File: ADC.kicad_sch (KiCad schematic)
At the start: 5 parts, among them J1 Conn_01x03_Socket, J11 Conn_01x03_Socket, J12 Conn_01x03_Socket, J13 Conn_01x03_Socket, U4 ADS1115IDGS

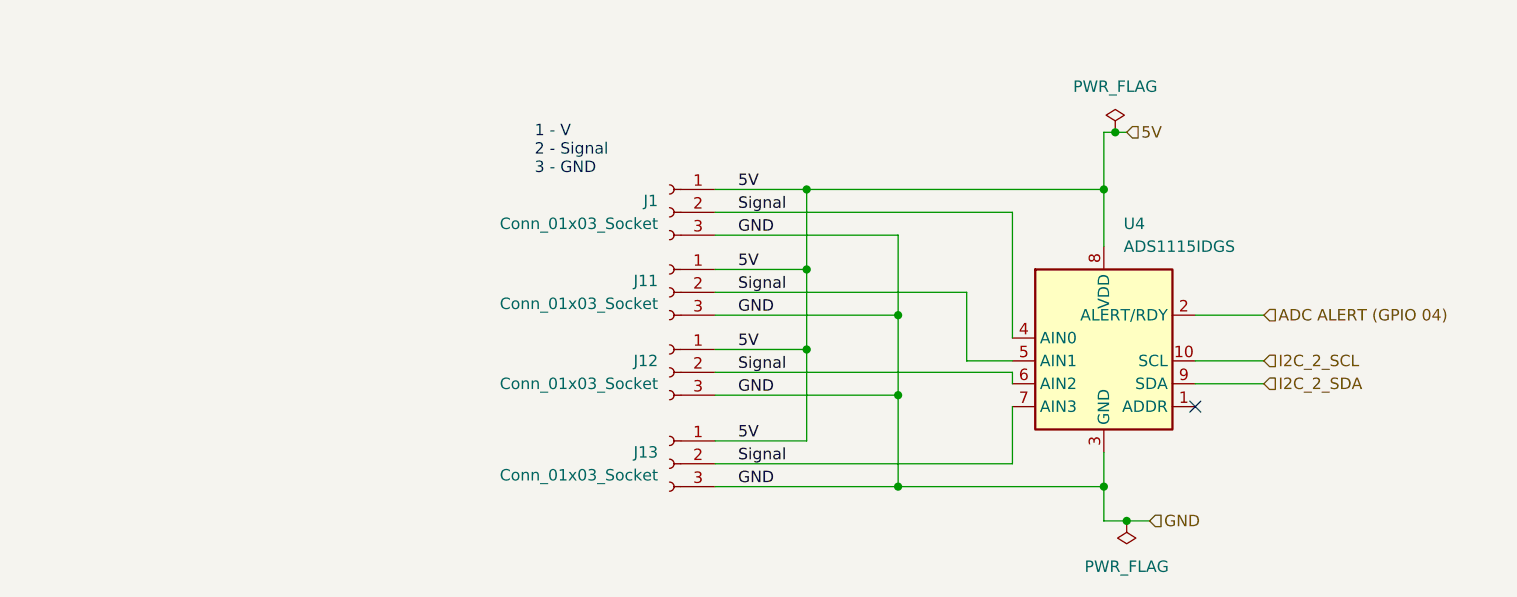
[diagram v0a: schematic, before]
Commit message: Replaced sockets with terminal blocks
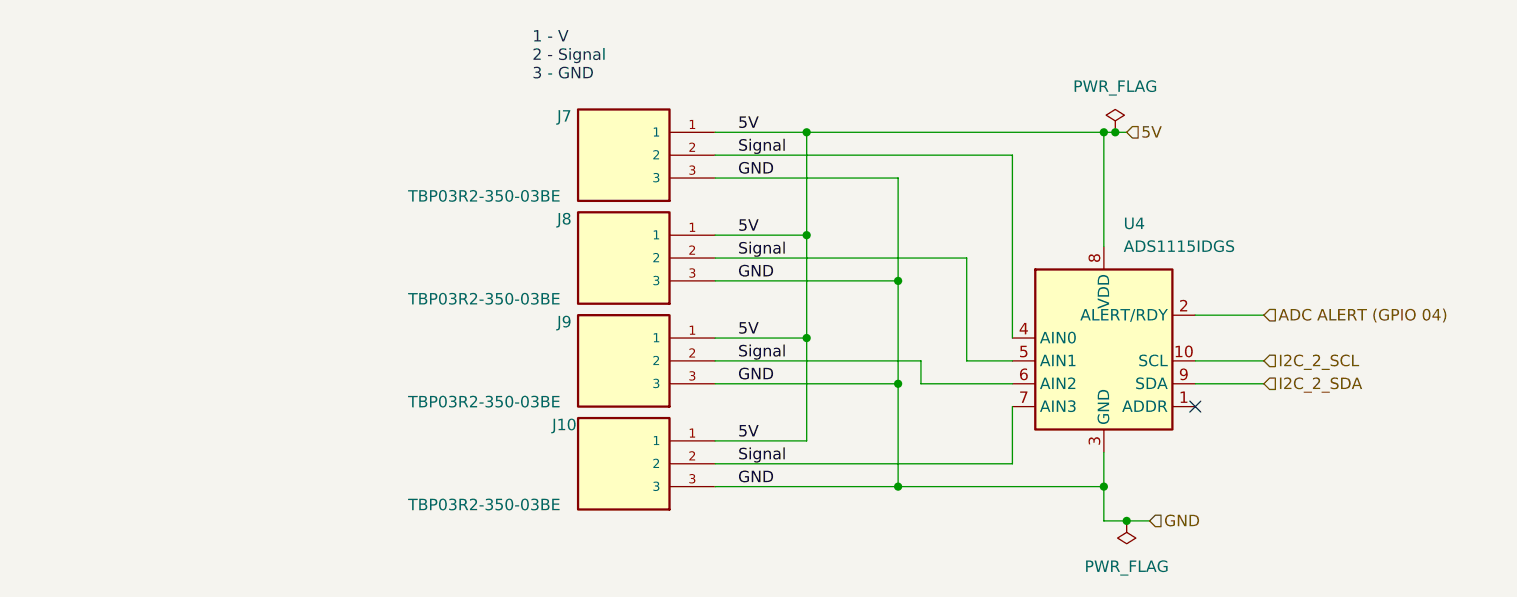
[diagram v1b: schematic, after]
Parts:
- removed J1, J11, J12, J13: Conn_01x03_Socket, symbol Connector:Conn_01x03_Socket
- added J10, J7, J8, J9: TBP03R2-350-03BE, TBP03R2-350-03BE:CUI_TBP03R2-350-03BE, symbol TBP03R2-350-03BE:TBP03R2-350-03BE
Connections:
- net 5V: now also J10.1, J7.1, J8.1, J9.1
- net GND: now also J10.3, J7.3, J8.3, J9.3
- net Signal: now also J10.2, J7.2, J8.2, J9.2

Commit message: Reorganized schematic and resolved ERC errors
Resolved some of the ERC errors related to disconnected pins and power flags. Renamed GPIO pins on 40-pin header. Changed ADC power supply to 3.3V and schmitt trigger circuit power supply to 5V. Connected 5V, 3.3V, and GND pins of 40-pin header. Assigned footprint for 40-pin header based on dimensions of expansion header on Jetson Nano Carrier Board.

Also moved IMU and 40-pin header KiCAD project files into their own folders.
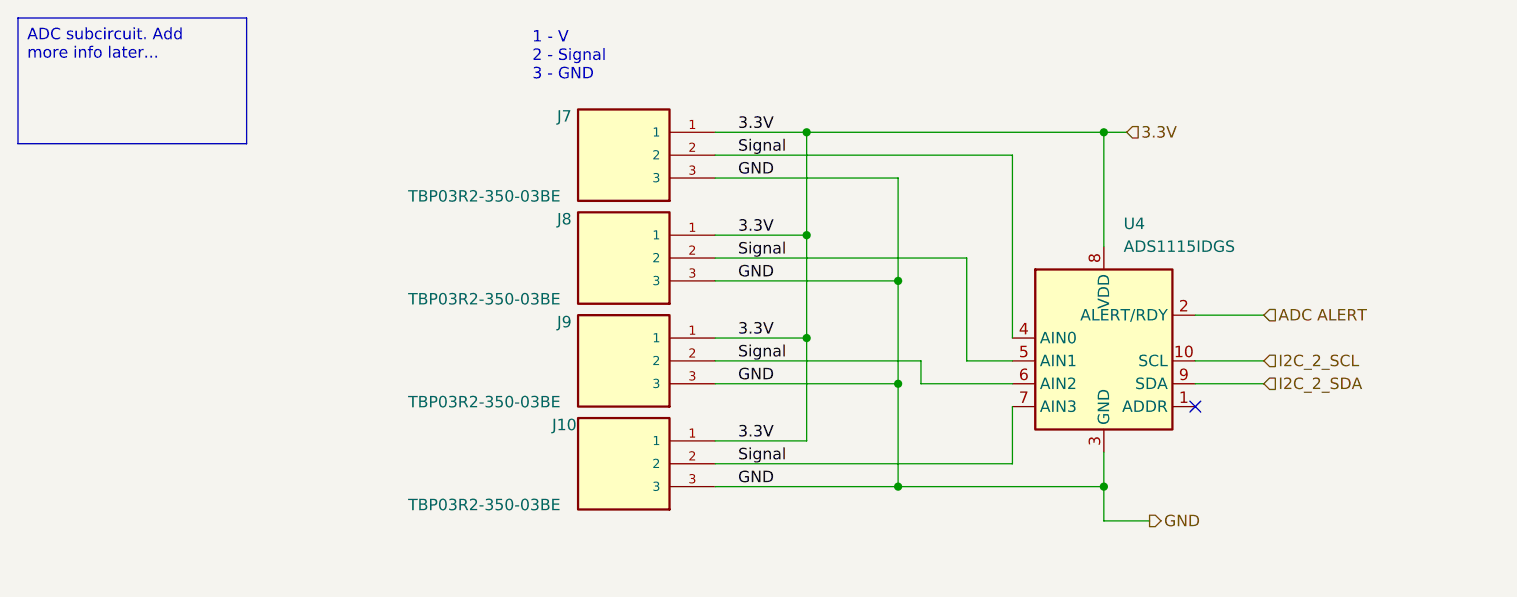
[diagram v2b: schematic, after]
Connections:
- net 5V renamed 3.3V
- net ADC ALERT (GPIO 04) renamed ADC ALERT

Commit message: Started PCB Layout
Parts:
- J10, J7, J8, J9: footprint TBP03R2-350-03BE:CUI_TBP03R2-350-03BE -> TBP03R2_350_03BE:CUI_TBP03R2-350-03BE
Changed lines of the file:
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@@
 			)
 		)
-		(property "Footprint" "TBP03R2-350-03BE:CUI_TBP03R2-350-03BE"
+		(property "Footprint" "TBP03R2_350_03BE:CUI_TBP03R2-350-03BE"
 			(at 96.52 73.66 0)
 			(effects
@@
 			)
 		)
-		(property "Footprint" "TBP03R2-350-03BE:CUI_TBP03R2-350-03BE"
+		(property "Footprint" "TBP03R2_350_03BE:CUI_TBP03R2-350-03BE"
 			(at 96.52 50.8 0)
 			(effects
@@
 			)
 		)
-		(property "Footprint" "TBP03R2-350-03BE:CUI_TBP03R2-350-03BE"
+		(property "Footprint" "TBP03R2_350_03BE:CUI_TBP03R2-350-03BE"
 			(at 96.52 62.23 0)
 			(effects
@@
 			)
 		)
-		(property "Footprint" "TBP03R2-350-03BE:CUI_TBP03R2-350-03BE"
+		(property "Footprint" "TBP03R2_350_03BE:CUI_TBP03R2-350-03BE"
 			(at 96.52 85.09 0)
 			(effects
